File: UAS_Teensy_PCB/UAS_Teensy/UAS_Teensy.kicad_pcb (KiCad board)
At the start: 2 copper layers, 50.8 x 50.8 mm, 11 parts, among them J1 UAS-rescue_SM02B-PASS-TBT(LF)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, J2 SM04B-GHS-TB(LF)(SN)-, J3 SM07B-GHS-TB(LF)(SN), J4 SM07B-GHS-TB(LF)(SN), J5 SM04B-GHS-TB(LF)(SN)-, J6 SM04B-GHS-TB(LF)(SN)-, J7 SM04B-GHS-TB(LF)(SN)-, U1 Teensy4.0, U2 BNO055

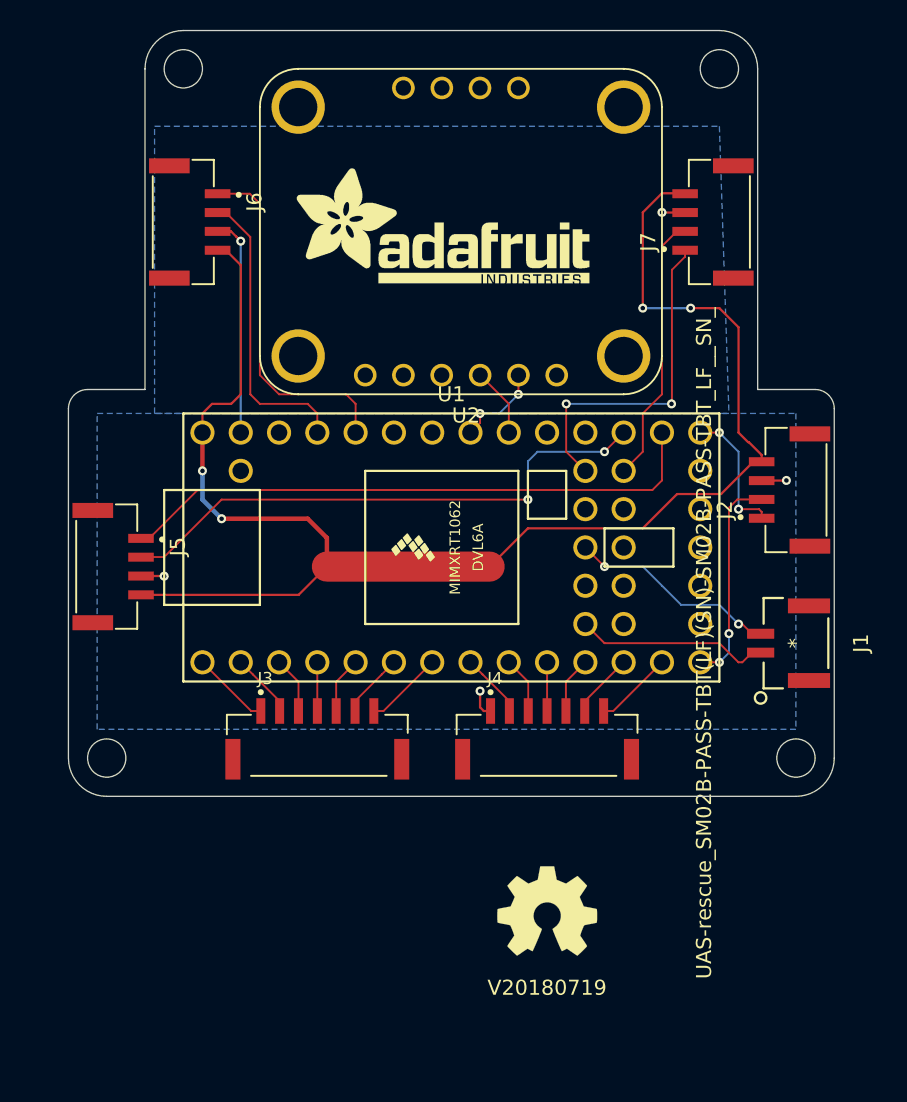
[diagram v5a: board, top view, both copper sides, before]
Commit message: trace changes and fill for teensy pcb
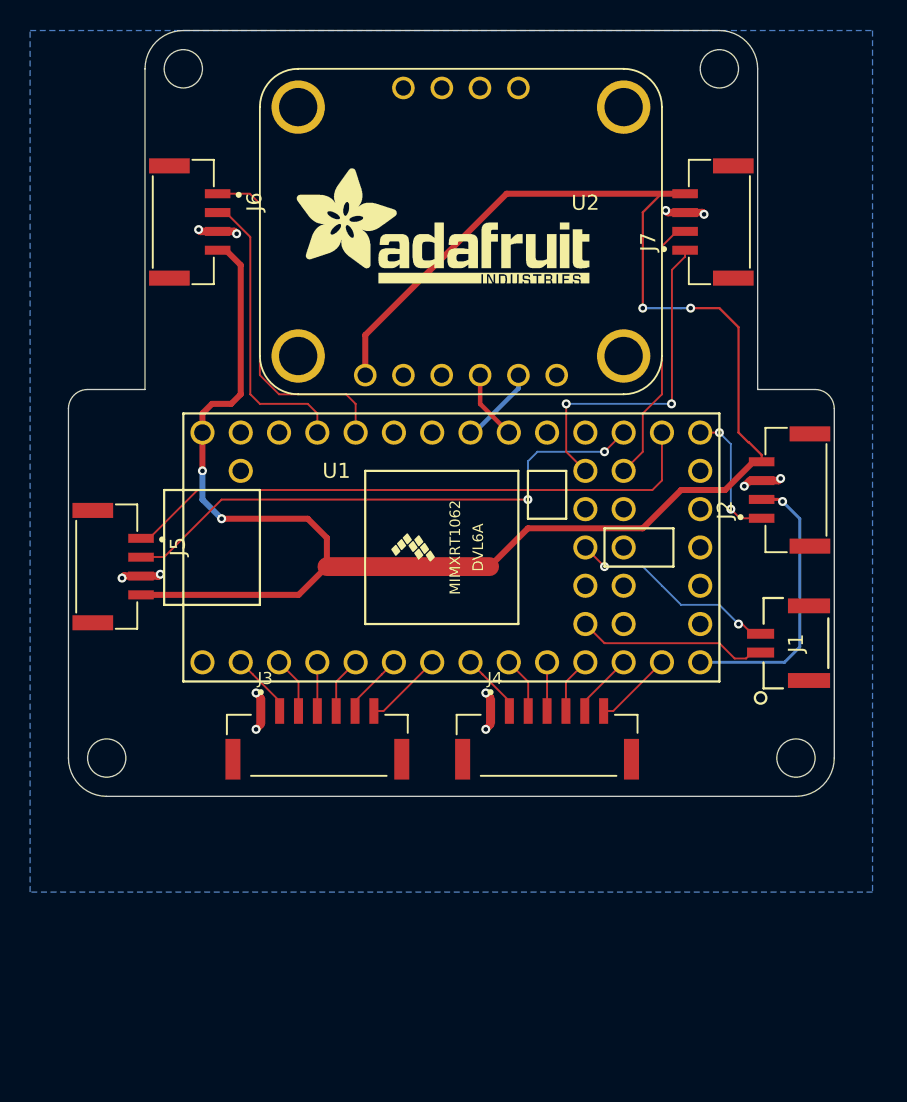
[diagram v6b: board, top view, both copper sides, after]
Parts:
- removed N1: OHWLOGO, Symbols:OSHW-Symbol_6.7x6mm_SilkScreen
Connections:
- U2 pad 1: Net-(U2-Pad1) -> 5V
- U2 pad 12: Net-(U1-Pad25) -> (no net)
- U2 pad 13: Net-(U1-Pad26) -> (no net)
- U2 pad 3: Net-(U2-Pad3) -> GND
- U2 pad 4: (no net) -> Net-(U1-Pad25)
- U2 pad 5: (no net) -> Net-(U1-Pad26)
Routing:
- net 5V: track 101.5 -> 129.2 mm
- net GND: track 26.3 -> 15.9 mm, vias 5 -> 12
- net Net-(J2-Pad2): track 14.2 -> 18.6 mm, vias 2 -> 1
- net Net-(U1-Pad26): track 5.87 -> 5.28 mm, vias 2 -> 0

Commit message: Teensy Board Updates
Teensy Board Updates
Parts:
- J3, J4: footprint UAS_Teensy:JST_SM07B-GHS-TB(LF)(SN) -> UAS_Teensy:JST_SM08B-GHS-TB(LF)(SN)
- moved J3 1.42 mm to (95.9, 99.1)
- moved J4 1.42 mm to (111.1, 99.1)
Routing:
- net Net-(J4-Pad7): track 5.21 -> 6.52 mm
- net Net-(J1-Pad2): track 14.0 -> 15.2 mm, vias 2 -> 0
- net Net-(J3-Pad7): track 5.21 -> 5.89 mm
- net Net-(J5-Pad2): track 36.9 -> 37.0 mm, vias 2 -> 1

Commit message: power in duh
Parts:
- moved J5 5.11 mm to (81.8, 83.8)
- moved J2 0.51 mm to (126.5, 83.8)
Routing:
- net 5V: track 129.2 -> 116.5 mm
- net Net-(J5-Pad2): track 37.0 -> 30.1 mm
- net Net-(J5-Pad1): track 39.3 -> 34.2 mm
- net GND: track 15.7 -> 12.2 mm, vias 12 -> 9
- net Net-(J2-Pad2): track 18.6 -> 19.3 mm
- net Net-(J2-Pad1): track 8.96 -> 8.45 mm, vias 2 -> 1
